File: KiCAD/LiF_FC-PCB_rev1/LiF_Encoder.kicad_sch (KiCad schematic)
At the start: 10 parts, among them J36 ENC 3V3_{EN}, U17 SN74HC14DR

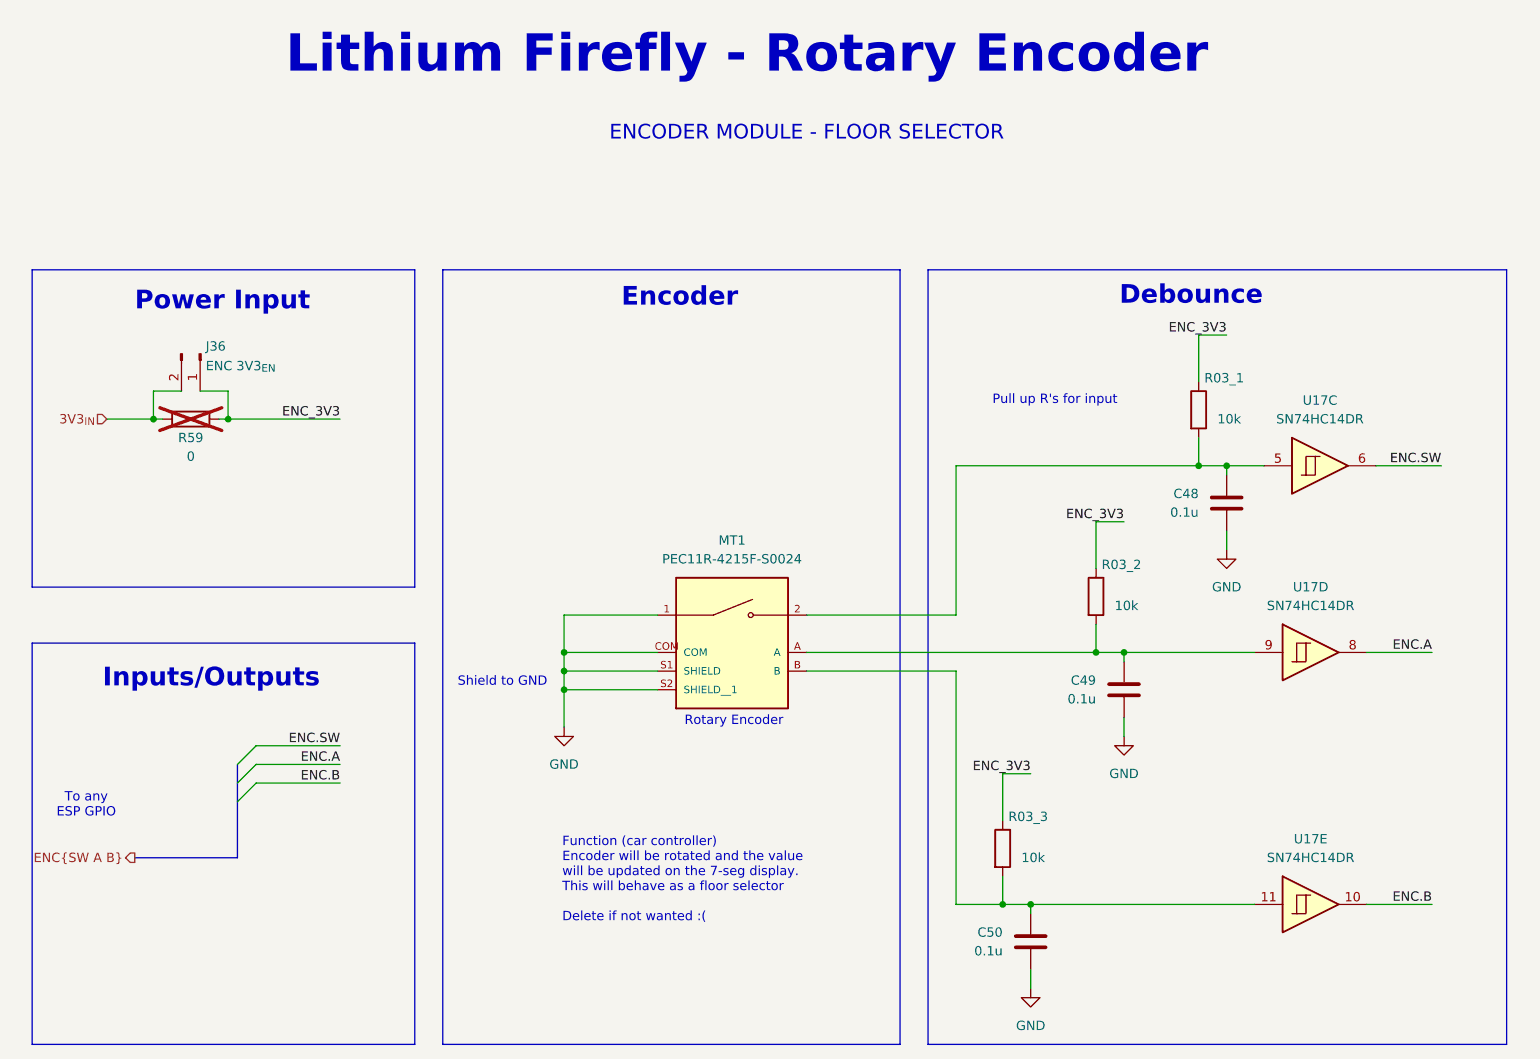
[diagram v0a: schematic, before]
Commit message: Added MCU pinout, shanged shift registers to GPIO expanders to save pins on MCU
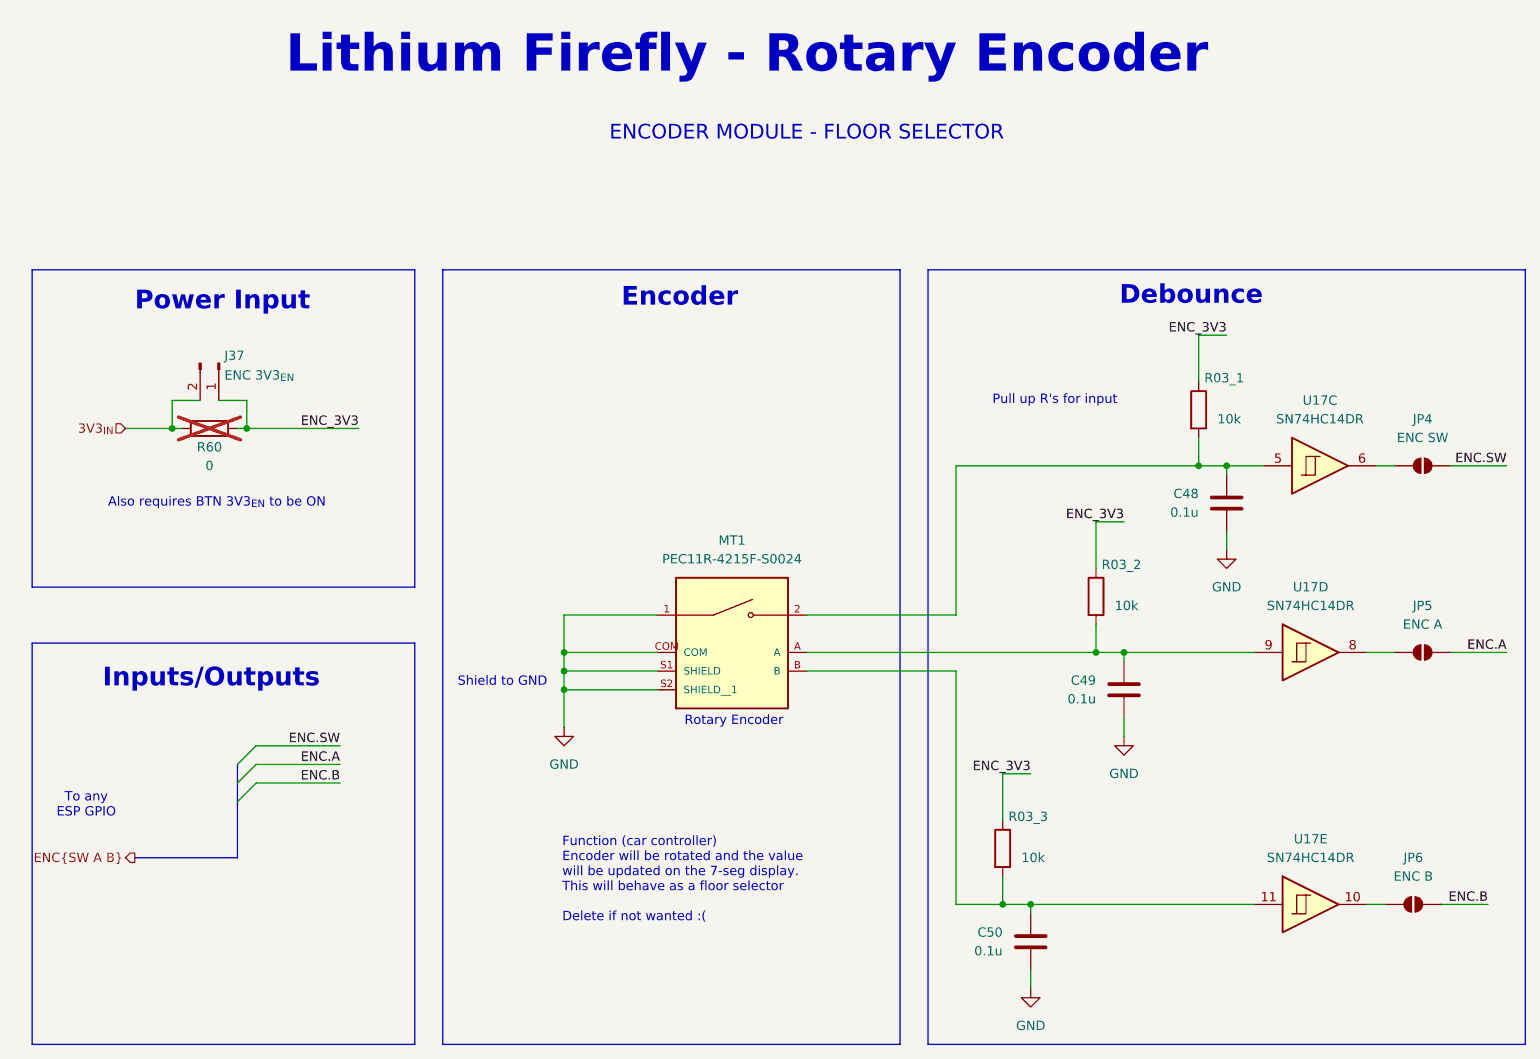
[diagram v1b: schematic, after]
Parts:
- added JP4: ENC SW, Jumper:SolderJumper-2_P1.3mm_Open_RoundedPad1.0x1.5mm, symbol Jumper:SolderJumper_2_Open
- added JP5: ENC A, Jumper:SolderJumper-2_P1.3mm_Open_RoundedPad1.0x1.5mm, symbol Jumper:SolderJumper_2_Open
- added JP6: ENC B, Jumper:SolderJumper-2_P1.3mm_Open_RoundedPad1.0x1.5mm, symbol Jumper:SolderJumper_2_Open
- renumbered J36 to J37, R59 to R60
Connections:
- net ENC.A: now also JP5.2 (B); no longer U17.8
- net ENC.B: now also JP6.2 (B); no longer U17.10
- net ENC.SW: now also JP4.2 (B); no longer U17.6
- new net: JP4.1 (A), U17.6
- new net: JP5.1 (A), U17.8
- new net: JP6.1 (A), U17.10
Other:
- note added: "Also requires BTN 3V3_{EN} to be ON"
- title: (none) -> Lithium Firefly Custom FC/CC PCB
- moved on the sheet: J37, R60

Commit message: Finalized schematic diagram. Only needs formatting fixes and resistor component sourcing info
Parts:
- renumbered C48 to C54, C49 to C55, C50 to C56, J37 to J39, R03_1 to R71, R60 to R72, R03_2 to R73, R03_3 to R74, U17 to U16
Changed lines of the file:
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@@
 		(on_board yes)
 		(dnp no)
-		(property "Reference" "C48"
+		(property "Reference" "C54"
 			(at 204.47 80.0099 0)
 			(effects
@@
 			(project "LiF_FC-PCB_rev1"
 				(path "/9e3e8da7-e506-46c9-90e5-307e4ad30d29/42a8ae4d-a2ee-470b-ba60-96ca330bd4df"
-					(reference "C48")
+					(reference "C54")
 					(unit 1)
 				)
@@
 		(dnp no)
 		(fields_autoplaced yes)
-		(property "Reference" "U17"
+		(property "Reference" "U16"
 			(at 220.98 67.31 0)
 			(effects
@@
 			(project "LiF_FC-PCB_rev1"
 				(path "/9e3e8da7-e506-46c9-90e5-307e4ad30d29/42a8ae4d-a2ee-470b-ba60-96ca330bd4df"
-					(reference "U17")
+					(reference "U16")
 					(unit 3)
 				)
@@
 		(on_board yes)
 		(dnp yes)
-		(property "Reference" "R60"
+		(property "Reference" "R72"
 			(at 69.85 73.66 90)
 			(effects
@@
 			(project "LiF_FC-PCB_rev1"
 				(path "/9e3e8da7-e506-46c9-90e5-307e4ad30d29/42a8ae4d-a2ee-470b-ba60-96ca330bd4df"
-					(reference "R60")
+					(reference "R72")
 					(unit 1)
 				)
@@
 		(on_board yes)
 		(dnp no)
-		(property "Reference" "R03_1"
+		(property "Reference" "R71"
 			(at 205.232 64.262 0)
 			(effects
@@
 			(project "LiF_FC-PCB_rev1"
 				(path "/9e3e8da7-e506-46c9-90e5-307e4ad30d29/42a8ae4d-a2ee-470b-ba60-96ca330bd4df"
-					(reference "R03_1")
+					(reference "R71")
 					(unit 1)
 				)
@@
 		(dnp no)
 		(fields_autoplaced yes)
-		(property "Reference" "#PWR0112"
+		(property "Reference" "#PWR0111"
 			(at 194.31 119.38 0)
 			(effects
@@
 			(project "LiF_FC-PCB_rev1"
 				(path "/9e3e8da7-e506-46c9-90e5-307e4ad30d29/42a8ae4d-a2ee-470b-ba60-96ca330bd4df"
-					(reference "#PWR0112")
+					(reference "#PWR0111")
 					(unit 1)
 				)
@@
 		(on_board yes)
 		(dnp no)
-		(property "Reference" "R03_3"
+		(property "Reference" "R74"
 			(at 178.562 123.952 0)
 			(effects
@@
 			(project "LiF_FC-PCB_rev1"
 				(path "/9e3e8da7-e506-46c9-90e5-307e4ad30d29/42a8ae4d-a2ee-470b-ba60-96ca330bd4df"
-					(reference "R03_3")
+					(reference "R74")
 					(unit 1)
 				)
@@
 		(on_board yes)
 		(dnp no)
-		(property "Reference" "C50"
+		(property "Reference" "C56"
 			(at 177.8 139.6999 0)
 			(effects
@@
 			(project "LiF_FC-PCB_rev1"
 				(path "/9e3e8da7-e506-46c9-90e5-307e4ad30d29/42a8ae4d-a2ee-470b-ba60-96ca330bd4df"
-					(reference "C50")
+					(reference "C56")
 					(unit 1)
 				)
@@
 		(on_board yes)
 		(dnp no)
-		(property "Reference" "R03_2"
+		(property "Reference" "R73"
 			(at 191.262 89.662 0)
 			(effects
@@
 			(project "LiF_FC-PCB_rev1"
 				(path "/9e3e8da7-e506-46c9-90e5-307e4ad30d29/42a8ae4d-a2ee-470b-ba60-96ca330bd4df"
-					(reference "R03_2")
+					(reference "R73")
 					(unit 1)
 				)
@@
 		(on_board yes)
 		(dnp no)
-		(property "Reference" "J37"
+		(property "Reference" "J39"
 			(at 71.882 61.214 90)
 			(effects
@@
 			(project "LiF_FC-PCB_rev1"
 				(path "/9e3e8da7-e506-46c9-90e5-307e4ad30d29/42a8ae4d-a2ee-470b-ba60-96ca330bd4df"
-					(reference "J37")
+					(reference "J39")
 					(unit 1)
 				)
@@
 		(dnp no)
 		(fields_autoplaced yes)
-		(property "Reference" "#PWR0111"
+		(property "Reference" "#PWR0110"
 			(at 118.11 118.11 0)
 			(effects
@@
 			(project "LiF_FC-PCB_rev1"
 				(path "/9e3e8da7-e506-46c9-90e5-307e4ad30d29/42a8ae4d-a2ee-470b-ba60-96ca330bd4df"
-					(reference "#PWR0111")
+					(reference "#PWR0110")
 					(unit 1)
 				)
@@
 		(dnp no)
 		(fields_autoplaced yes)
-		(property "Reference" "#PWR0113"
+		(property "Reference" "#PWR0112"
 			(at 181.61 153.67 0)
 			(effects
@@
 			(project "LiF_FC-PCB_rev1"
 				(path "/9e3e8da7-e506-46c9-90e5-307e4ad30d29/42a8ae4d-a2ee-470b-ba60-96ca330bd4df"
-					(reference "#PWR0113")
+					(reference "#PWR0112")
 					(unit 1)
 				)
@@
 		(on_board yes)
 		(dnp no)
-		(property "Reference" "C49"
+		(property "Reference" "C55"
 			(at 190.5 105.4099 0)
 			(effects
@@
 			(project "LiF_FC-PCB_rev1"
 				(path "/9e3e8da7-e506-46c9-90e5-307e4ad30d29/42a8ae4d-a2ee-470b-ba60-96ca330bd4df"
-					(reference "C49")
+					(reference "C55")
 					(unit 1)
 				)
@@
 		(dnp no)
 		(fields_autoplaced yes)
-		(property "Reference" "#PWR0110"
+		(property "Reference" "#PWR0109"
 			(at 208.28 93.98 0)
 			(effects
@@
 			(project "LiF_FC-PCB_rev1"
 				(path "/9e3e8da7-e506-46c9-90e5-307e4ad30d29/42a8ae4d-a2ee-470b-ba60-96ca330bd4df"
-					(reference "#PWR0110")
+					(reference "#PWR0109")
 					(unit 1)
 				)
@@
 		(dnp no)
 		(fields_autoplaced yes)
-		(property "Reference" "U17"
+		(property "Reference" "U16"
 			(at 219.71 127 0)
 			(effects
@@
 			(project "LiF_FC-PCB_rev1"
 				(path "/9e3e8da7-e506-46c9-90e5-307e4ad30d29/42a8ae4d-a2ee-470b-ba60-96ca330bd4df"
-					(reference "U17")
+					(reference "U16")
 					(unit 5)
 				)
@@
 		(dnp no)
 		(fields_autoplaced yes)
-		(property "Reference" "U17"
+		(property "Reference" "U16"
 			(at 219.71 92.71 0)
 			(effects
@@
 			(project "LiF_FC-PCB_rev1"
 				(path "/9e3e8da7-e506-46c9-90e5-307e4ad30d29/42a8ae4d-a2ee-470b-ba60-96ca330bd4df"
-					(reference "U17")
+					(reference "U16")
 					(unit 4)
 				)

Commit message: backup before leaving school
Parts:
- J39: footprint Connector_PinHeader_2.54mm:PinHeader_1x02_P2.54mm_Vertical -> Connector_PinHeader_2.54mm:PinHeader_1x02_P2.54mm_Vertical_SMD_Pin1Left
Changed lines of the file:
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@@
 			)
 		)
-		(property "Footprint" "Connector_PinHeader_2.54mm:PinHeader_1x02_P2.54mm_Vertical"
+		(property "Footprint" "Connector_PinHeader_2.54mm:PinHeader_1x02_P2.54mm_Vertical_SMD_Pin1Left"
 			(at 71.12 62.23 0)
 			(effects

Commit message: backup before splitting the schematics into 2 boards: I/O PCB and Service PCB
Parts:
- removed JP4: ENC SW, Jumper:SolderJumper-2_P1.3mm_Open_RoundedPad1.0x1.5mm, symbol Jumper:SolderJumper_2_Open
- removed JP5: ENC A, Jumper:SolderJumper-2_P1.3mm_Open_RoundedPad1.0x1.5mm, symbol Jumper:SolderJumper_2_Open
- removed JP6: ENC B, Jumper:SolderJumper-2_P1.3mm_Open_RoundedPad1.0x1.5mm, symbol Jumper:SolderJumper_2_Open
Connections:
- net ENC.A: now also U16.8
- net ENC.B: now also U16.10
- net ENC.SW: now also U16.6
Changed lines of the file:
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@@
 	(wire
 		(pts
-			(xy 228.6 76.2) (xy 231.14 76.2)
+			(xy 228.6 76.2) (xy 246.38 76.2)
 		)
 		(stroke
@@
 	(wire
 		(pts
-			(xy 238.76 76.2) (xy 246.38 76.2)
-		)
-		(stroke
-			(width 0)
-			(type default)
-		)
-	)
-	(wire
-		(pts
 			(xy 58.42 71.12) (xy 64.77 71.12)
 		)
@@
 	(wire
 		(pts
-			(xy 227.33 135.89) (xy 229.87 135.89)
+			(xy 227.33 135.89) (xy 243.84 135.89)
 		)
 		(stroke
@@
 	(wire
 		(pts
-			(xy 227.33 101.6) (xy 231.14 101.6)
+			(xy 227.33 101.6) (xy 246.38 101.6)
 		)
 		(stroke
@@
 		)
 	)
-	(wire
-		(pts
-			(xy 238.76 101.6) (xy 246.38 101.6)
-		)
-		(stroke
-			(width 0)
-			(type default)
-		)
-	)
 	(bus
 		(pts
@@
 		(pts
 			(xy 130.81 96.52) (xy 118.11 96.52)
-		)
-		(stroke
-			(width 0)
-			(type default)
-		)
-	)
-	(wire
-		(pts
-			(xy 237.49 135.89) (xy 243.84 135.89)
 		)
 		(stroke
@@
 	)
 	(symbol
-		(lib_id "Jumper:SolderJumper_2_Open")
-		(at 234.95 76.2 0)
-		(unit 1)
-		(exclude_from_sim no)
-		(in_bom no)
-		(on_board yes)
-		(dnp no)
-		(fields_autoplaced yes)
-		(property "Reference" "JP4"
-			(at 234.95 69.85 0)
-			(effects
-				(font
-					(size 1.27 1.27)
-				)
-			)
-		)
-		(property "Value" "ENC SW"
-			(at 234.95 72.39 0)
-			(effects
-				(font
-					(size 1.27 1.27)
-				)
-			)
-		)
-		(property "Footprint" "Jumper:SolderJumper-2_P1.3mm_Open_RoundedPad1.0x1.5mm"
-			(at 234.95 76.2 0)
-			(effects
-				(font
-					(size 1.27 1.27)
-				)
-				(hide yes)
-			)
-		)
-		(property "Datasheet" "~"
-			(at 234.95 76.2 0)
-			(effects
-				(font
-					(size 1.27 1.27)
-				)
-				(hide yes)
-			)
-		)
-		(property "Description" "Solder Jumper, 2-pole, open"
-			(at 234.95 76.2 0)
-			(effects
-				(font
-					(size 1.27 1.27)
-				)
-				(hide yes)
-			)
-		)
-		(pin "2"
-		)
-		(pin "1"
-		)
-		(instances
-			(project "LiF_FC-PCB_rev1"
-				(path "/9e3e8da7-e506-46c9-90e5-307e4ad30d29/42a8ae4d-a2ee-470b-ba60-96ca330bd4df"
-					(reference "JP4")
-					(unit 1)
-				)
-			)
-		)
-	)
-	(symbol
 		(lib_id "power:GND")
 		(at 194.31 113.03 0)
@@
 	)
 	(symbol
-		(lib_id "Jumper:SolderJumper_2_Open")
-		(at 234.95 101.6 0)
-		(unit 1)
-		(exclude_from_sim no)
-		(in_bom no)
-		(on_board yes)
-		(dnp no)
-		(fields_autoplaced yes)
-		(property "Reference" "JP5"
-			(at 234.95 95.25 0)
-			(effects
-				(font
-					(size 1.27 1.27)
-				)
-			)
-		)
-		(property "Value" "ENC A"
-			(at 234.95 97.79 0)
-			(effects
-				(font
-					(size 1.27 1.27)
-				)
-			)
-		)
-		(property "Footprint" "Jumper:SolderJumper-2_P1.3mm_Open_RoundedPad1.0x1.5mm"
-			(at 234.95 101.6 0)
-			(effects
-				(font
-					(size 1.27 1.27)
-				)
-				(hide yes)
-			)
-		)
-		(property "Datasheet" "~"
-			(at 234.95 101.6 0)
-			(effects
-				(font
-					(size 1.27 1.27)
-				)
-				(hide yes)
-			)
-		)
-		(property "Description" "Solder Jumper, 2-pole, open"
-			(at 234.95 101.6 0)
-			(effects
-				(font
-					(size 1.27 1.27)
-				)
-				(hide yes)
-			)
-		)
-		(pin "2"
-		)
-		(pin "1"
-		)
-		(instances
-			(project "LiF_FC-PCB_rev1"
-				(path "/9e3e8da7-e506-46c9-90e5-307e4ad30d29/42a8ae4d-a2ee-470b-ba60-96ca330bd4df"
-					(reference "JP5")
-					(unit 1)
-				)
-			)
-		)
-	)
-	(symbol
 		(lib_id "power:GND")
 		(at 208.28 87.63 0)
@@
 				)
 			)
-		)
-	)
-	(symbol
-		(lib_id "Jumper:SolderJumper_2_Open")
-		(at 233.68 135.89 0)
-		(unit 1)
-		(exclude_from_sim no)
-		(in_bom no)
-		(on_board yes)
-		(dnp no)
-		(fields_autoplaced yes)
-		(property "Reference" "JP6"
-			(at 233.68 129.54 0)
-			(effects
-				(font
-					(size 1.27 1.27)
-				)
-			)
-		)
-		(property "Value" "ENC B"
-			(at 233.68 132.08 0)
-			(effects
-				(font
-					(size 1.27 1.27)
-				)
-			)
-		)
-		(property "Footprint" "Jumper:SolderJumper-2_P1.3mm_Open_RoundedPad1.0x1.5mm"
-			(at 233.68 135.89 0)
-			(effects
-				(font
-					(size 1.27 1.27)
-				)
-				(hide yes)
-			)
-		)
-		(property "Datasheet" "~"
-			(at 233.68 135.89 0)
-			(effects
-				(font
-					(size 1.27 1.27)
-				)
-				(hide yes)
-			)
-		)
-		(property "Description" "Solder Jumper, 2-pole, open"
-			(at 233.68 135.89 0)
-			(effects
-				(font
-					(size 1.27 1.27)
-				)
-				(hide yes)
-			)
-		)
-		(pin "2"
-		)
-		(pin "1"
-		)
-		(instances
-			(project ""
-				(path "/9e3e8da7-e506-46c9-90e5-307e4ad30d29/42a8ae4d-a2ee-470b-ba60-96ca330bd4df"
-					(reference "JP6")
-					(unit 1)
-				)
-			)
